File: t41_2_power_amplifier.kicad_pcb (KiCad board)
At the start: 2 copper layers, 78 x 93 mm, 46 parts, among them J1 5-1814832-1, J2 5-1814832-1, J3 B2B-XH-A_LF__SN_, J5 Screw_Terminal_01x02, Q1 Q_NMOS_GSD, Q3 Q_NMOS_GSD, T1 Transformer_1P_SS, T2 Transformer_1P_1S, T3 Transformer_1P_1S, U1 MCP1802x-xx02xOT

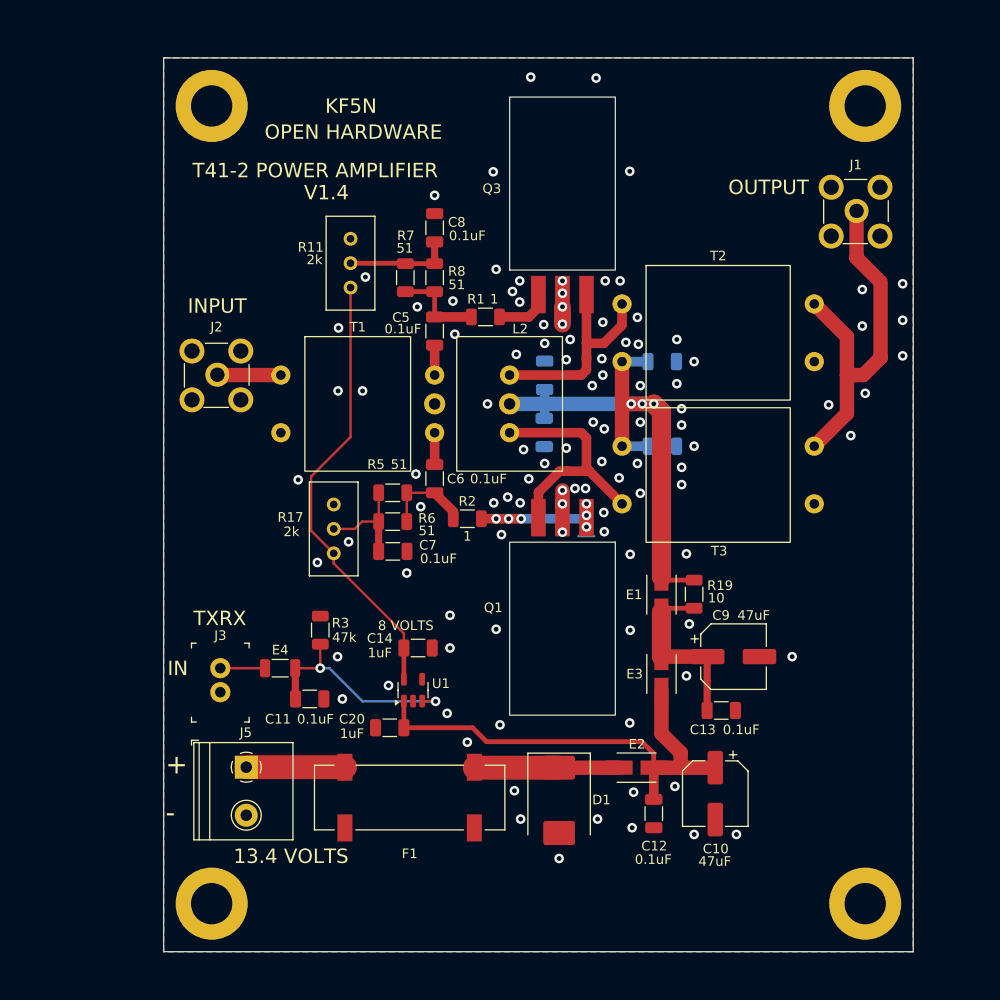
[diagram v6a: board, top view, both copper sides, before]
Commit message: Added notes to schematic.
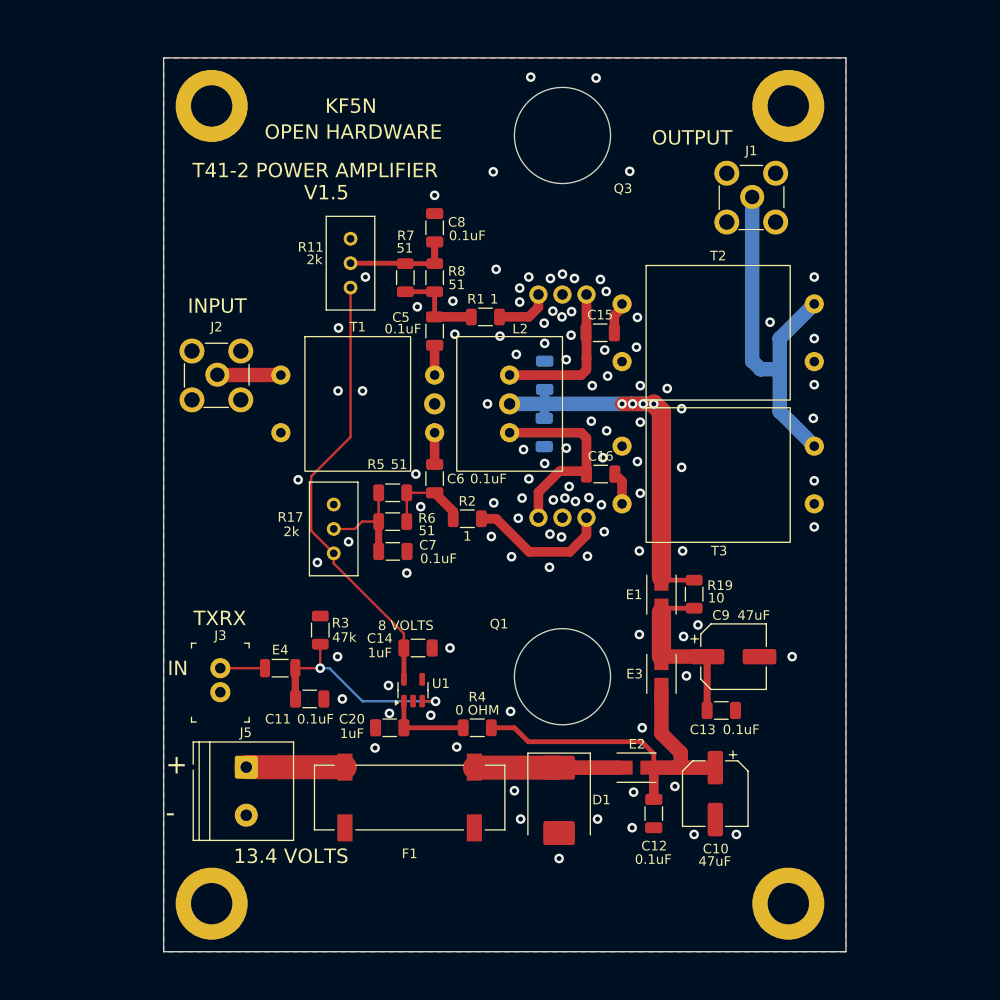
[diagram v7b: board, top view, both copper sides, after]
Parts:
- added R4: 0 OHM, Resistor_SMD:R_1206_3216Metric, F.Cu at (147.6, 123.7)
- C15, C16: moved to F.Cu
- Q1, Q3: footprint TO-220_RF:TO-220_RF_Flat -> TO-220_RF:TO-220_RF_Flat_Through_Hole
- moved J1 11.0 mm to (176.1, 68.5)
- moved H3 8.00 mm to (180.0, 142.0)
- moved H4 8.00 mm to (180.0, 59.0)
- moved C15 7.11 mm to (160.4, 82.6)
- moved C16 7.05 mm to (160.5, 97.3)
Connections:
- C15 pad 1: /12V_PA -> Net-(Q3-D)
- C15 pad 2: GND -> Net-(T2-AA)
- C16 pad 1: /12V_PA -> Net-(Q1-D)
- C16 pad 2: GND -> Net-(T3-AB)
- C20 pad 1: /12V_FIL -> Net-(U1-VIN)
- T2 pad 1: Net-(Q3-D) -> Net-(T2-AA)
- T2 pad 2: /12V_PA -> GND
- T3 pad 1: /12V_PA -> GND
- T3 pad 2: Net-(Q1-D) -> Net-(T3-AB)
- U1 pad 1: /12V_FIL -> Net-(U1-VIN)
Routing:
- net /12V_PA: track 57.3 -> 43.2 mm, vias 3 -> 4
- net /12V_FIL: track 49.9 -> 38.0 mm
- net GND: track 9.65 -> 0.30 mm
- net Net-(U1-VIN): track 0.00 -> 8.99 mm
- net Net-(Q3-D): track 23.3 -> 16.6 mm
- net Net-(Q1-D): track 26.1 -> 20.2 mm
- net Net-(T3-AB): track 0.00 -> 3.41 mm
- net Net-(T2-AA): track 0.00 -> 3.33 mm
- net Net-(Q1-G): track 17.9 -> 14.9 mm, vias 6 -> 0
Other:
- board size 78 x 93 mm -> 71 x 93 mm
- board text added: "V1.5"
- board text removed: "V1.4"

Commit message: Version 1.6 first commit.
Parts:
- moved C16 3.47 mm to (157.0, 97.3)
- moved Q1 1.50 mm to (155.0, 112.9)
- moved Q3 1.50 mm to (155.0, 67.6)
- moved C15 1.45 mm to (159.0, 82.6)
- moved J1 1.40 mm to (174.7, 68.5)
- moved T2 1.40 mm to (171.3, 82.6)
- moved T3 1.40 mm to (171.3, 97.4)
- moved C1 1.15 mm to (153.5, 87.0)
- moved R4 1.14 mm to (146.5, 123.7)
- moved C4 1.10 mm to (153.5, 93.0)
- moved L2 1.00 mm to (150.0, 90.0)
- moved R2 0.60 mm to (146.0, 102.0)
- moved H1 0.50 mm to (120.5, 59.0)
- moved H2 0.50 mm to (120.5, 142.0)
- moved R1 0.49 mm to (148.0, 81.0)
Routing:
- net Net-(Q1-D): track 20.2 -> 13.7 mm
- net Net-(Q3-D): track 16.6 -> 13.5 mm
- net Net-(Q1-G): track 14.9 -> 13.0 mm
- net Net-(Q3-G): track 5.91 -> 4.05 mm
- net Net-(T3-AB): track 3.41 -> 4.27 mm
- net /12V_PA: track 43.2 -> 43.8 mm, vias 4 -> 3
- net GND: track 0.30 -> 0.00 mm, vias 105 -> 102
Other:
- board size 71 x 93 mm -> 69.5 x 93 mm
